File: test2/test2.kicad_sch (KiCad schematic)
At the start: 0 parts

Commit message: Added Resistor and LED
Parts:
- added D1: LED, symbol Device:LED
- added R1: R, symbol Device:R
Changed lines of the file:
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@@
 		(comment 5 "c1000")
+	)
+	(symbol
+		(lib_id "Device:R")
+		(at 144.78 85.09 0)
+		(unit 1)
+		(body_style 1)
+		(exclude_from_sim no)
+		(in_bom yes)
+		(on_board yes)
+		(in_pos_files yes)
+		(dnp no)
+		(fields_autoplaced yes)
+		(property "Reference" "R1"
+			(at 147.32 83.8199 0)
+			(show_name no)
+			(do_not_autoplace no)
+			(effects
+				(font
+					(size 1.27 1.27)
+				)
+				(justify left)
+			)
+		)
+		(property "Value" "R"
+			(at 147.32 86.3599 0)
+			(show_name no)
+			(do_not_autoplace no)
+			(effects
+				(font
+					(size 1.27 1.27)
+				)
+				(justify left)
+			)
+		)
+		(property "Footprint" ""
+			(at 143.002 85.09 90)
+			(hide yes)
+			(show_name no)
+			(do_not_autoplace no)
+			(effects
+				(font
+					(size 1.27 1.27)
+				)
+			)
+		)
+		(property "Datasheet" ""
+			(at 144.78 85.09 0)
+			(hide yes)
+			(show_name no)
+			(do_not_autoplace no)
+			(effects
+				(font
+					(size 1.27 1.27)
+				)
+			)
+		)
+		(property "Description" "Resistor"
+			(at 144.78 85.09 0)
+			(hide yes)
+			(show_name no)
+			(do_not_autoplace no)
+			(effects
+				(font
+					(size 1.27 1.27)
+				)
+			)
+		)
+		(pin "2"
+		)
+		(pin "1"
+		)
+		(instances
+			(project "test2"
+				(path "/a16b2917-54e0-4f71-a869-9bcc0622af1e"
+					(reference "R1")
+					(unit 1)
+				)
+			)
+		)
+	)
+	(symbol
+		(lib_id "Device:LED")
+		(at 105.41 90.17 0)
+		(unit 1)
+		(body_style 1)
+		(exclude_from_sim no)
+		(in_bom yes)
+		(on_board yes)
+		(in_pos_files yes)
+		(dnp no)
+		(fields_autoplaced yes)
+		(property "Reference" "D1"
+			(at 103.8225 83.82 0)
+			(show_name no)
+			(do_not_autoplace no)
+			(effects
+				(font
+					(size 1.27 1.27)
+				)
+			)
+		)
+		(property "Value" "LED"
+			(at 103.8225 86.36 0)
+			(show_name no)
+			(do_not_autoplace no)
+			(effects
+				(font
+					(size 1.27 1.27)
+				)
+			)
+		)
+		(property "Footprint" ""
+			(at 105.41 90.17 0)
+			(hide yes)
+			(show_name no)
+			(do_not_autoplace no)
+			(effects
+				(font
+					(size 1.27 1.27)
+				)
+			)
+		)
+		(property "Datasheet" ""
+			(at 105.41 90.17 0)
+			(hide yes)
+			(show_name no)
+			(do_not_autoplace no)
+			(effects
+				(font
+					(size 1.27 1.27)
+				)
+			)
+		)
+		(property "Description" "Light emitting diode"
+			(at 105.41 90.17 0)
+			(hide yes)
+			(show_name no)
+			(do_not_autoplace no)
+			(effects
+				(font
+					(size 1.27 1.27)
+				)
+			)
+		)
+		(property "Sim.Pins" "1=K 2=A"
+			(at 105.41 90.17 0)
+			(hide yes)
+			(show_name no)
+			(do_not_autoplace no)
+			(effects
+				(font
+					(size 1.27 1.27)
+				)
+			)
+		)
+		(pin "2"
+		)
+		(pin "1"
+		)
+		(instances
+			(project "test2"
+				(path "/a16b2917-54e0-4f71-a869-9bcc0622af1e"
+					(reference "D1")
+					(unit 1)
+				)
+			)
+		)
 	)
 	(sheet_instances

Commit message: + Wire Connection
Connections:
- net at R1.2: now also D1.2 (A)
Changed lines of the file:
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@@
 		(comment 5 "c1000")
+	)
+	(wire
+		(pts
+			(xy 109.22 90.17) (xy 144.78 90.17)
+		)
+		(stroke
+			(width 0)
+			(type default)
+		)
+	)
+	(wire
+		(pts
+			(xy 144.78 88.9) (xy 144.78 90.17)
+		)
+		(stroke
+			(width 0)
+			(type default)
+		)
 	)
 	(symbol

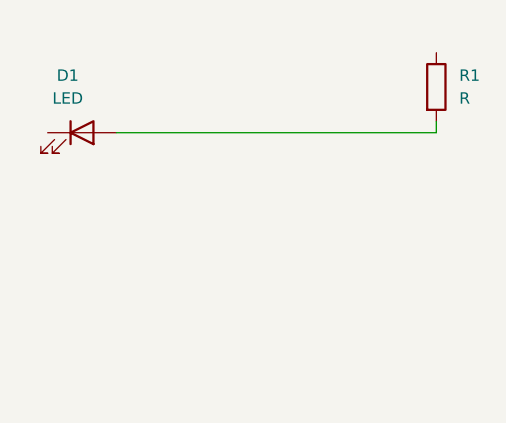
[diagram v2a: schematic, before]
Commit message: Moved LED and rotated resistor
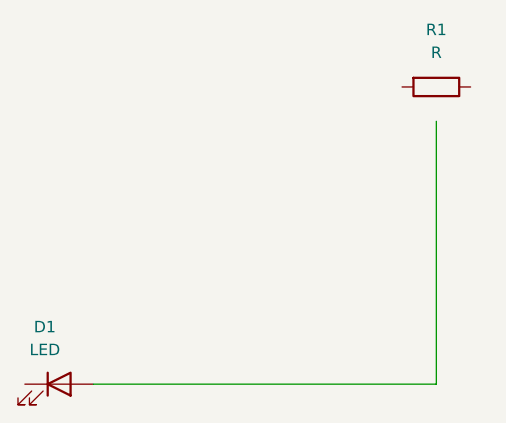
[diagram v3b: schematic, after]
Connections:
- net at R1.2: no longer D1.2 (A)
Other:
- moved on the sheet: D1, R1
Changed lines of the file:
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@@
 	(wire
 		(pts
-			(xy 109.22 90.17) (xy 144.78 90.17)
+			(xy 106.68 118.11) (xy 144.78 118.11)
 		)
 		(stroke
@@
 	(wire
 		(pts
-			(xy 144.78 88.9) (xy 144.78 90.17)
+			(xy 144.78 118.11) (xy 144.78 88.9)
 		)
 		(stroke
@@
 	(symbol
 		(lib_id "Device:R")
-		(at 144.78 85.09 0)
+		(at 144.78 85.09 270)
 		(unit 1)
 		(body_style 1)
@@
 		(fields_autoplaced yes)
 		(property "Reference" "R1"
-			(at 147.32 83.8199 0)
+			(at 144.78 78.74 90)
 			(show_name no)
 			(do_not_autoplace no)
@@
 					(size 1.27 1.27)
 				)
-				(justify left)
 			)
 		)
 		(property "Value" "R"
-			(at 147.32 86.3599 0)
+			(at 144.78 81.28 90)
 			(show_name no)
 			(do_not_autoplace no)
@@
 					(size 1.27 1.27)
 				)
-				(justify left)
 			)
 		)
 		(property "Footprint" ""
-			(at 143.002 85.09 90)
+			(at 144.78 83.312 90)
 			(hide yes)
 			(show_name no)
@@
 	(symbol
 		(lib_id "Device:LED")
-		(at 105.41 90.17 0)
+		(at 102.87 118.11 0)
 		(unit 1)
 		(body_style 1)
@@
 		(fields_autoplaced yes)
 		(property "Reference" "D1"
-			(at 103.8225 83.82 0)
+			(at 101.2825 111.76 0)
 			(show_name no)
 			(do_not_autoplace no)
@@
 		)
 		(property "Value" "LED"
-			(at 103.8225 86.36 0)
+			(at 101.2825 114.3 0)
 			(show_name no)
 			(do_not_autoplace no)
@@
 		)
 		(property "Footprint" ""
-			(at 105.41 90.17 0)
+			(at 102.87 118.11 0)
 			(hide yes)
 			(show_name no)
@@
 		)
 		(property "Datasheet" ""
-			(at 105.41 90.17 0)
+			(at 102.87 118.11 0)
 			(hide yes)
 			(show_name no)
@@
 		)
 		(property "Description" "Light emitting diode"
-			(at 105.41 90.17 0)
+			(at 102.87 118.11 0)
 			(hide yes)
 			(show_name no)
@@
 		)
 		(property "Sim.Pins" "1=K 2=A"
-			(at 105.41 90.17 0)
+			(at 102.87 118.11 0)
 			(hide yes)
 			(show_name no)
